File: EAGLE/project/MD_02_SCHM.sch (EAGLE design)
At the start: 48 parts, among them IC1 CA3140D, IC2 CA3140D, IC3 CD74HC4067M96E4, IC4 CD74HC4067M96E4, IC5 ADS1113IDGSR

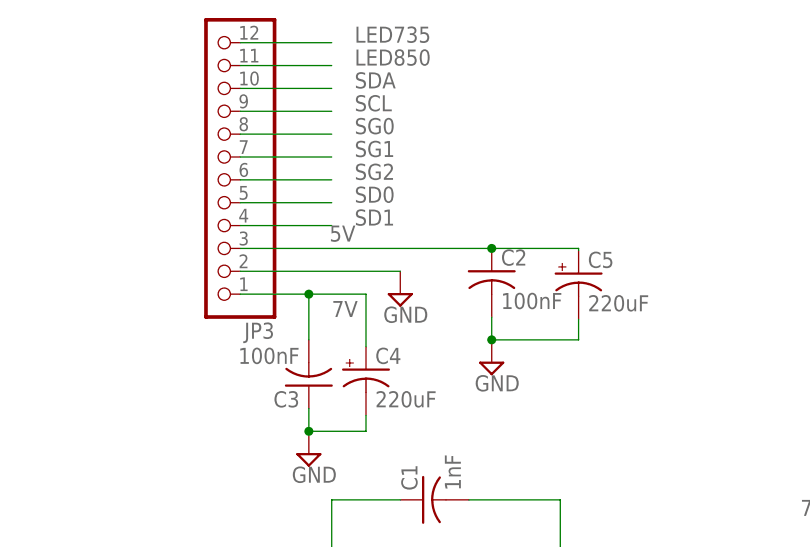
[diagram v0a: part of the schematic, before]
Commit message: Updating EAGLE files and top/bottom layers PDF
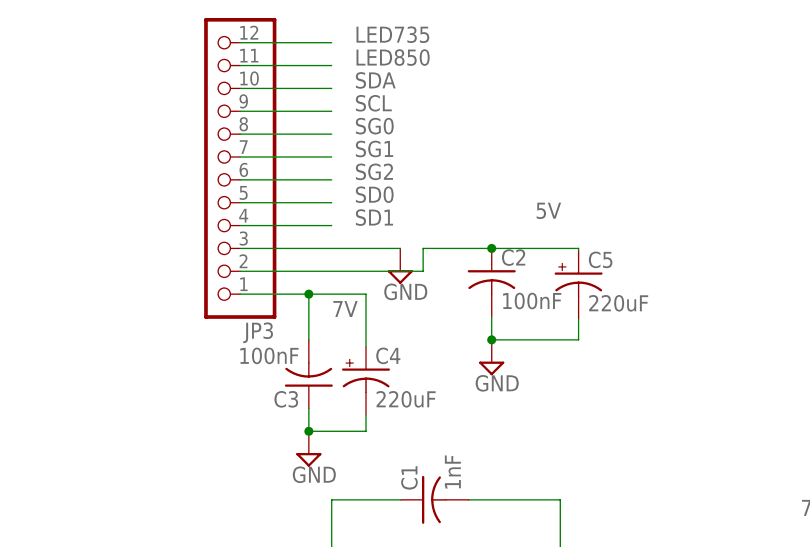
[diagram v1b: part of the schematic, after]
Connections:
- net 5V: now also JP3.2; no longer JP3.3
- net GND: now also JP3.3; no longer JP3.2
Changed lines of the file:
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@@
 <attribute name="VALUE" x="13.97" y="121.92" size="1.778" layer="96" rot="R180"/>
 </instance>
-<instance part="SUPPLY10" gate="GND" x="27.94" y="88.9" smashed="yes">
-<attribute name="VALUE" x="26.035" y="85.725" size="1.778" layer="96"/>
+<instance part="SUPPLY10" gate="GND" x="27.94" y="91.44" smashed="yes">
+<attribute name="VALUE" x="26.035" y="88.265" size="1.778" layer="96"/>
 </instance>
 <instance part="C2" gate="G$1" x="38.1" y="91.44" smashed="yes">
@@
 </segment>
 <segment>
-<wire x1="10.16" y1="91.44" x2="27.94" y2="91.44" width="0.1524" layer="91"/>
-<pinref part="SUPPLY10" gate="GND" pin="GND"/>
-<pinref part="JP3" gate="G$1" pin="2"/>
-</segment>
-<segment>
 <pinref part="SUPPLY11" gate="GND" pin="GND"/>
 <pinref part="C2" gate="G$1" pin="2"/>
@@
 <wire x1="24.13" y1="73.66" x2="17.78" y2="73.66" width="0.1524" layer="91"/>
 <junction x="17.78" y="73.66"/>
+</segment>
+<segment>
+<pinref part="JP3" gate="G$1" pin="3"/>
+<pinref part="SUPPLY10" gate="GND" pin="GND"/>
+<wire x1="10.16" y1="93.98" x2="27.94" y2="93.98" width="0.1524" layer="91"/>
 </segment>
 </net>
@@
 </segment>
 <segment>
-<label x="20.066" y="94.742" size="1.778" layer="95"/>
+<label x="42.926" y="97.282" size="1.778" layer="95"/>
 <pinref part="C2" gate="G$1" pin="1"/>
-<wire x1="10.16" y1="93.98" x2="38.1" y2="93.98" width="0.1524" layer="91"/>
 <pinref part="C5" gate="G$1" pin="+"/>
 <wire x1="47.752" y1="93.726" x2="47.752" y2="93.98" width="0.1524" layer="91"/>
 <wire x1="47.752" y1="93.98" x2="38.1" y2="93.98" width="0.1524" layer="91"/>
+<wire x1="38.1" y1="93.98" x2="30.48" y2="93.98" width="0.1524" layer="91"/>
 <junction x="38.1" y="93.98"/>
-<pinref part="JP3" gate="G$1" pin="3"/>
-</segment>
-</net>
+<wire x1="30.48" y1="93.98" x2="30.48" y2="91.44" width="0.1524" layer="91"/>
+<pinref part="JP3" gate="G$1" pin="2"/>
+<wire x1="30.48" y1="91.44" x2="10.16" y2="91.44" width="0.1524" layer="91"/>
+</segment>
+</net>

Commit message: Updated vias diameter and MUX footprint; Added GND vias; Polygon isolation changed to 24
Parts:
- removed IC4: CD74HC4067M96E4, SamacSys_Parts:CD74HC4067M96E4
- added IC6: CD74HC4067SM96, CD74HC4067SM96:CD74HC4067SM96
- IC3: value CD74HC4067M96E4 -> CD74HC4067SM96; device SamacSys_Parts:CD74HC4067M96E4 -> CD74HC4067SM96:CD74HC4067SM96
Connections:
- net 5V: now also IC6.VCC; no longer IC4.VCC
- net DET1: now also IC6.I2; no longer IC3.I2
- net DET2: now also IC6.I1; no longer IC3.I1
- net DET3: now also IC6.I0; no longer IC3.I0
- net G1: now also IC3.I0; no longer IC4.I0
- net G2: now also IC3.I1; no longer IC4.I1
- net G3: now also IC3.I2; no longer IC4.I2
- net G4: now also IC3.I3; no longer IC4.I3
- net G5: now also IC3.I4; no longer IC4.I4
- net G6: now also IC3.I5; no longer IC4.I5
- net G7: now also IC3.I6; no longer IC4.I6
- net G8: now also IC3.I7; no longer IC4.I7
- net GND: now also IC6.!E, IC6.GND, IC6.S2, IC6.S3; no longer IC3.S2, IC4.!E, IC4.GND, IC4.S3
- net OUT: now also IC3.COMMON_INPUT/OUTPUT; no longer IC4.COMMON_INPUT/OUTPUT
- net SD0: now also IC6.S0; no longer IC3.S0
- net SD1: now also IC6.S1; no longer IC3.S1
- net SG0: now also IC3.S0; no longer IC4.S0
- net SG1: now also IC3.S1; no longer IC4.S1
- net SG2: now also IC3.S2; no longer IC4.S2
- net TIA-: now also IC6.COMMON_INPUT/OUTPUT; no longer IC3.COMMON_INPUT/OUTPUT
